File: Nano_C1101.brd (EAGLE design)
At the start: 45.4 x 44.4 mm, 7 parts

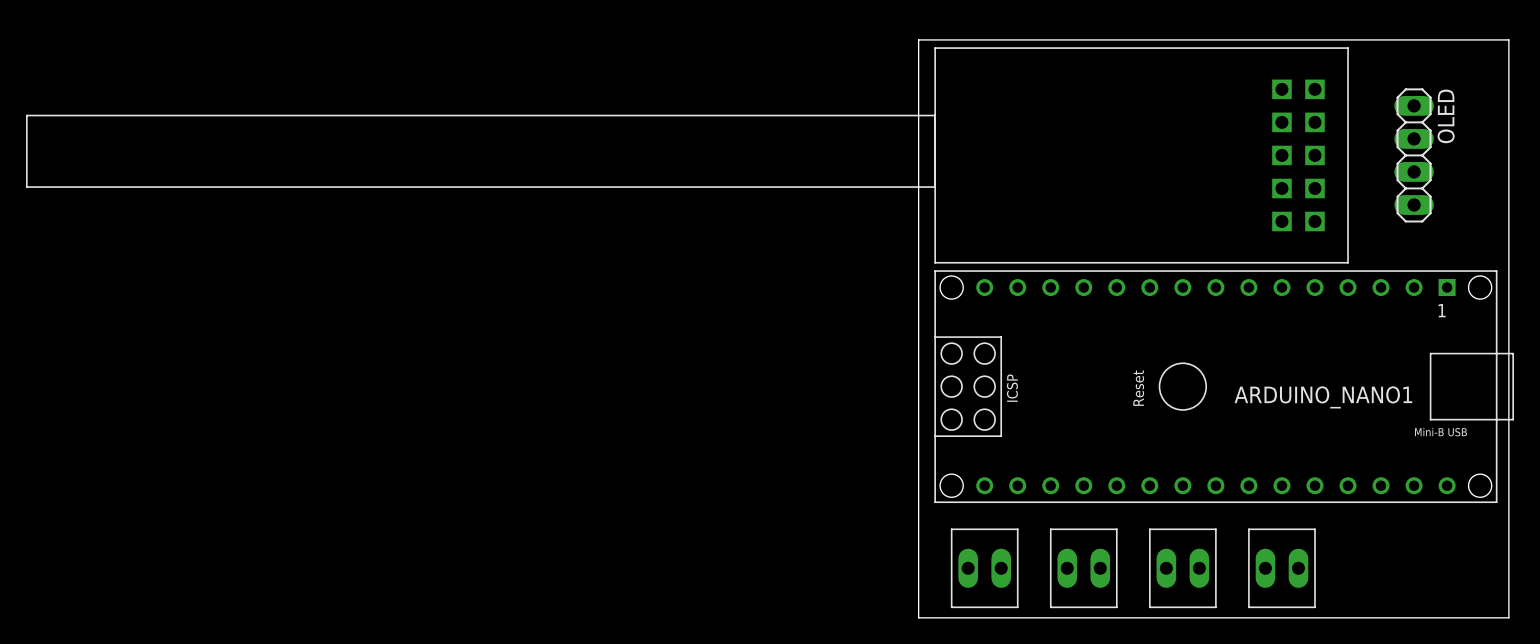
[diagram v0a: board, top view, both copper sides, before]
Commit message: few typos, 3V3 -> 5V
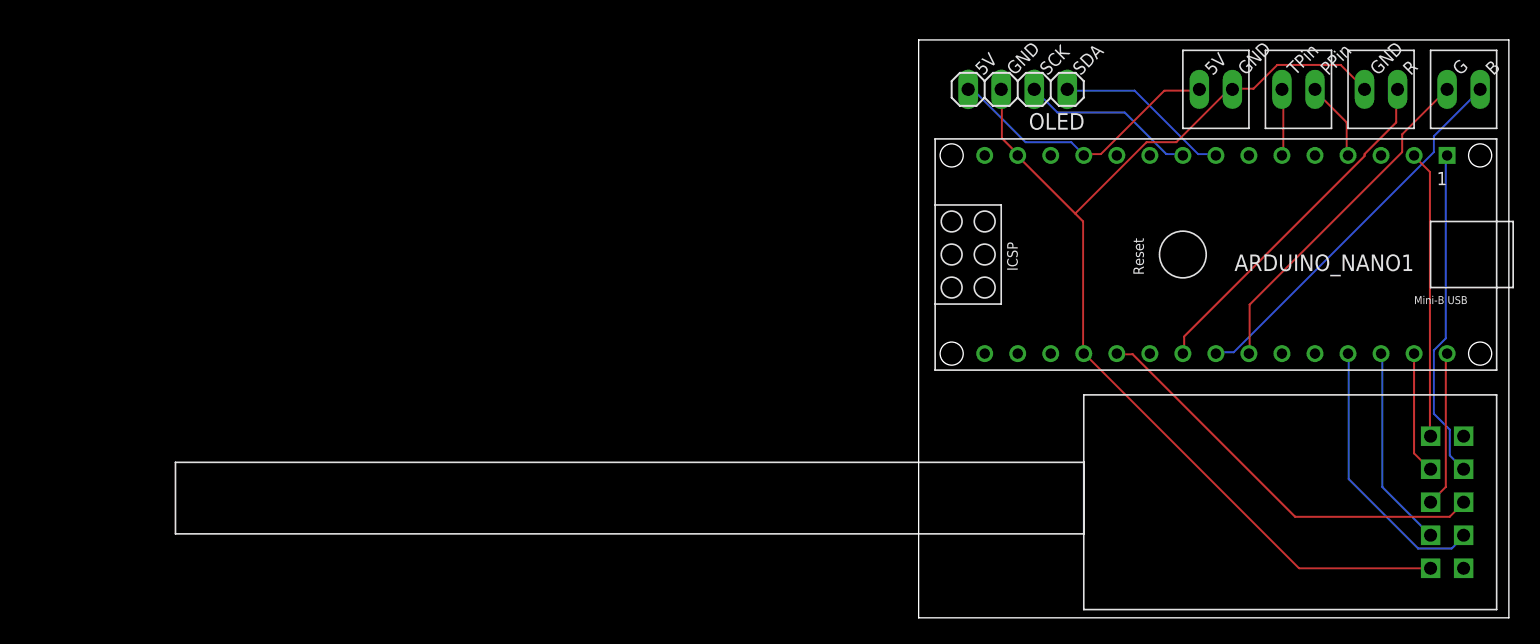
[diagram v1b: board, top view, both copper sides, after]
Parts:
- removed 3.3V--GND: CONRAD567588-2, johannes:CONRAD567588
- added 5V--GND: CONRAD567588-2, johannes:CONRAD567588
- moved TPIN--PPIN 40.4 mm to (29.2, 40.6)
- moved R--GND 39.9 mm to (35.6, 40.6), turned to 180 degrees
- moved G--B 39.4 mm to (41.9, 40.6)
- moved OLED 30.9 mm to (7.62, 40.6), turned to 180 degrees
- moved U$1 29.0 mm to (41.9, 3.81)
- moved ARDUINO_NANO1 10.2 mm to (20.3, 27.9)
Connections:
- net 3V3: no longer 3.3V--GND.P$1
- net 5V: now also 5V--GND.P$1
- net GND: now also 5V--GND.P$2; no longer 3.3V--GND.P$2
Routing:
- net GND: track 0.00 -> 84.2 mm
- net GDO2: track 0.00 -> 32.4 mm
- net B-RGB: track 0.00 -> 29.5 mm
- net R-RGB: track 0.00 -> 27.2 mm
- net G-RGB: track 0.00 -> 26.6 mm
- net SCLK: track 0.00 -> 25.5 mm
- net 3V3: track 0.00 -> 22.1 mm
- net 5V: track 0.00 -> 22.1 mm
- net GDO0: track 0.00 -> 21.2 mm
- net CSN: track 0.00 -> 15.6 mm
- net SDA: track 0.00 -> 13.7 mm
- net SCK: track 0.00 -> 13.6 mm
- net MISO: track 0.00 -> 12.0 mm
- net MOSI: track 0.00 -> 9.45 mm
- net PPIN: track 0.00 -> 6.13 mm
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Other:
- board text added: "5V"
- board text added: "B"
- board text added: "G"
- board text added: "GND"
- board text added: "PPin"
- board text added: "R"
- board text added: "SCK"
- board text added: "SDA"
- board text added: "TPin"

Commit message: Semi-final version of Nano_C1101
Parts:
- added JP1: (no value), adafruit:1X01
- moved 5V--GND 3.81 mm to (26.7, 40.6)
- moved TPIN--PPIN 2.54 mm to (31.8, 40.6)
- moved R--GND 1.27 mm to (36.8, 40.6)
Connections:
- new net N$1: ARDUINO_NANO1.24, JP1.1
- net G-RGB: now also ARDUINO_NANO1.25; no longer ARDUINO_NANO1.24
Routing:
- net N$1: track 0.00 -> 22.4 mm
- net 5V: track 22.1 -> 28.4 mm
- net GND: track 84.2 -> 90.3 mm
- net B-RGB: track 29.5 -> 31.6 mm
- net R-RGB: track 27.2 -> 28.9 mm
- net SCK: track 13.6 -> 14.8 mm
- net TPIN: track 5.16 -> 6.28 mm
- net G-RGB: track 26.6 -> 25.6 mm
- net PPIN: track 6.13 -> 5.16 mm

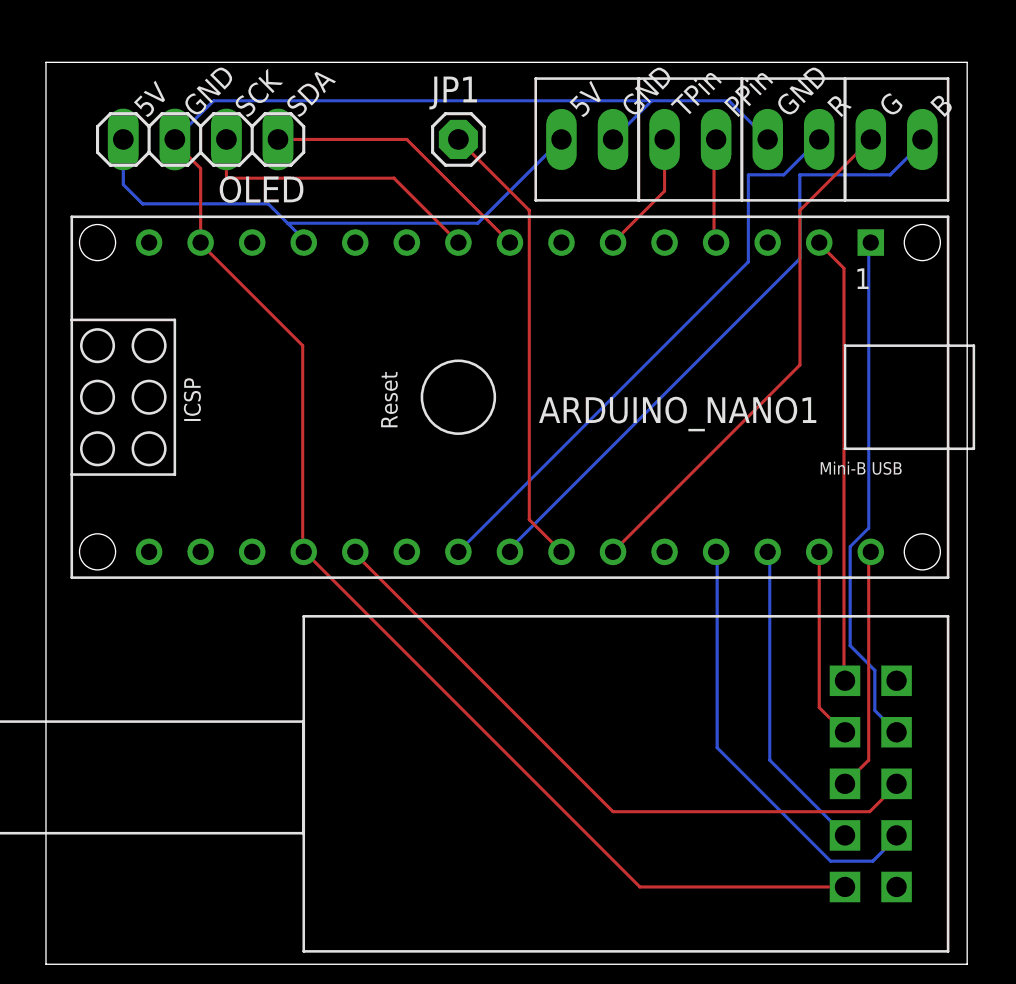
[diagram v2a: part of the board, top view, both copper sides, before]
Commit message: Added resistor and more pins for sensors
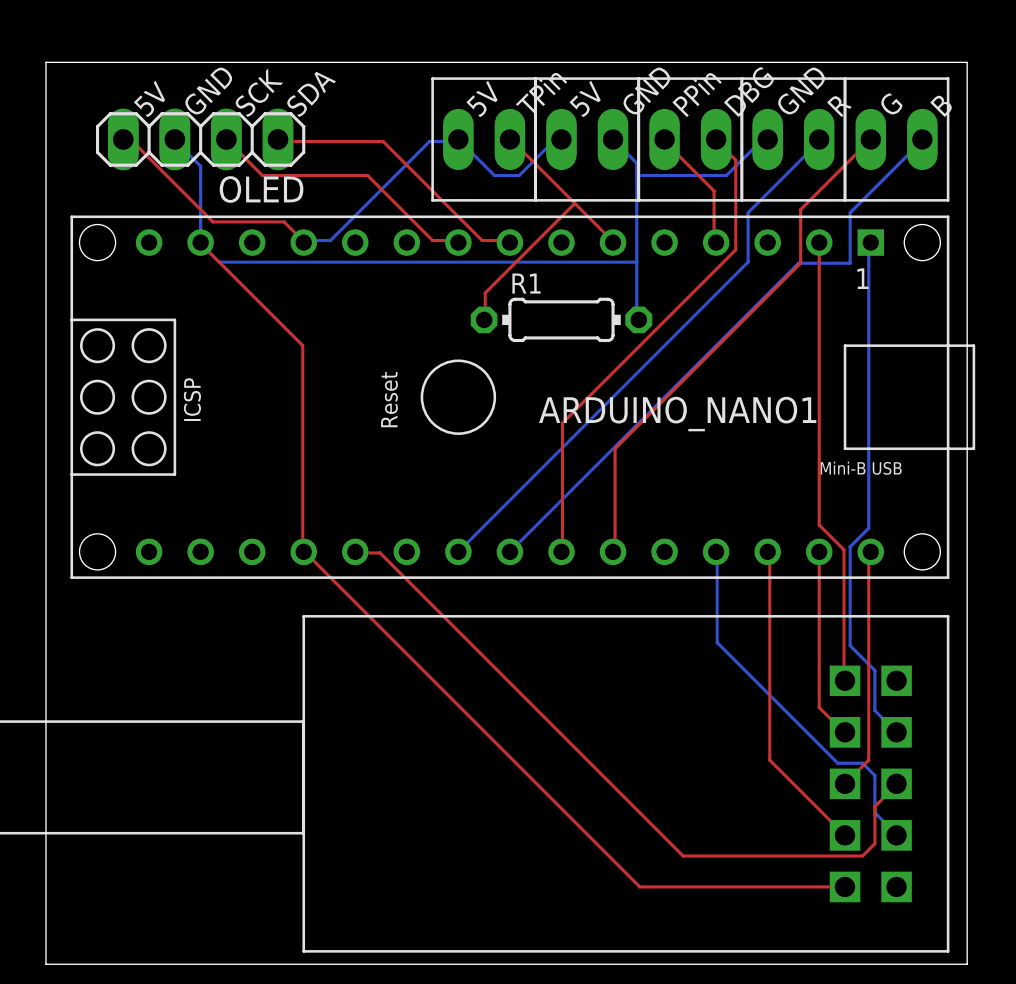
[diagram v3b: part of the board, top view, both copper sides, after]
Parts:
- removed JP1: (no value), adafruit:1X01
- added 5V-TPIN: CONRAD567588-2, johannes:CONRAD567588
- added R1: 1k, rcl:0204/7
- turned DEBUG--PPIN to 180 degrees
- renumbered TPIN--PPIN to DEBUG--PPIN
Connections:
- removed net N$1: ARDUINO_NANO1.24, JP1.1
- new net DEBUG: ARDUINO_NANO1.24, DEBUG--PPIN.P$1
- net 5V: now also 5V-TPIN.P$1
- net GND: now also R1.2
- net TPIN: now also 5V-TPIN.P$2, R1.1; no longer DEBUG--PPIN.P$1
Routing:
- net DEBUG: track 0.00 -> 24.3 mm
- net N$1: track 22.4 -> 0.00 mm
- net TPIN: track 6.28 -> 14.9 mm
- net GND: track 90.3 -> 95.0 mm
- net GDO0: track 21.4 -> 18.4 mm
- net GDO2: track 32.6 -> 35.5 mm
- net B-RGB: track 31.6 -> 30.2 mm
- net SCK: track 14.8 -> 13.6 mm
- net R-RGB: track 28.9 -> 27.7 mm
- net 5V: track 28.4 -> 27.4 mm
- net PPIN: track 5.16 -> 6.13 mm
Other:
- board text added: "DBG"

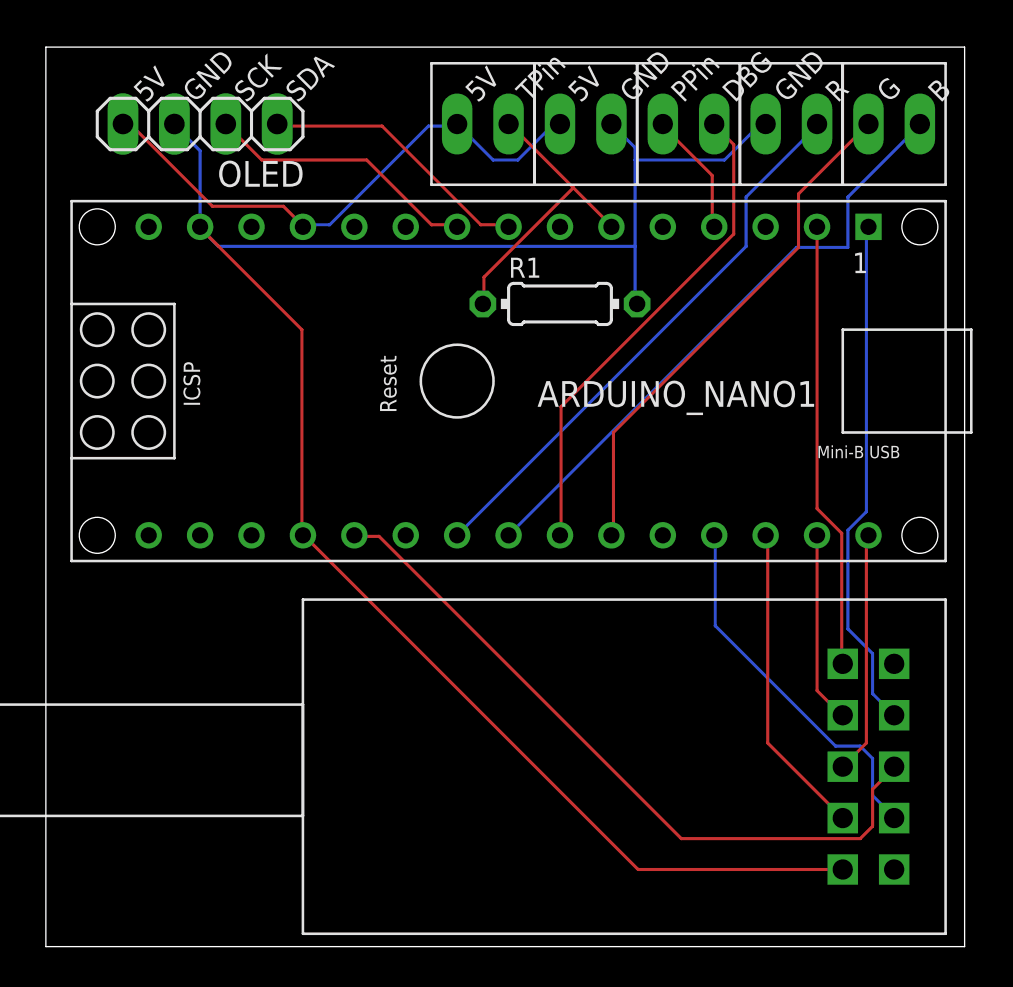
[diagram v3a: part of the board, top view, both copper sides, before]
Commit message: Some more clearance in Nano_C1101.brd
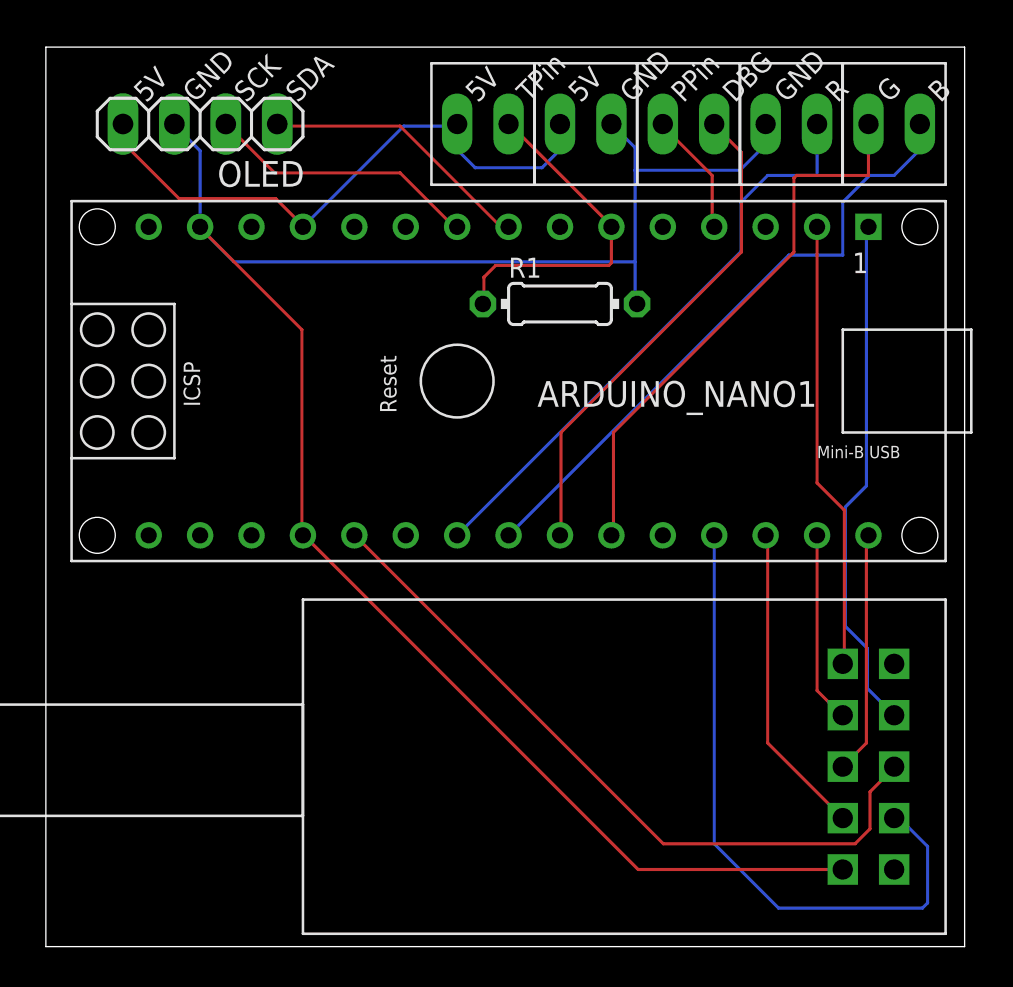
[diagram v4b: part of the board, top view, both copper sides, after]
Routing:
- net GDO0: track 18.4 -> 32.2 mm
- net 5V: track 27.4 -> 29.7 mm
- net TPIN: track 14.9 -> 17.0 mm
- net G-RGB: track 25.6 -> 27.7 mm
- net R-RGB: track 27.7 -> 29.1 mm
- net GND: track 95.0 -> 96.1 mm
- net B-RGB: track 30.2 -> 31.0 mm

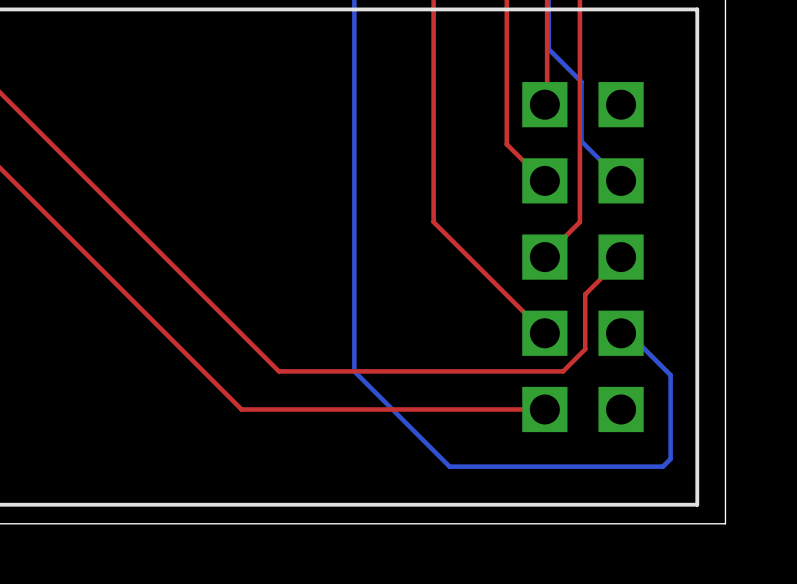
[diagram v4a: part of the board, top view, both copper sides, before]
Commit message: Added text on PCB
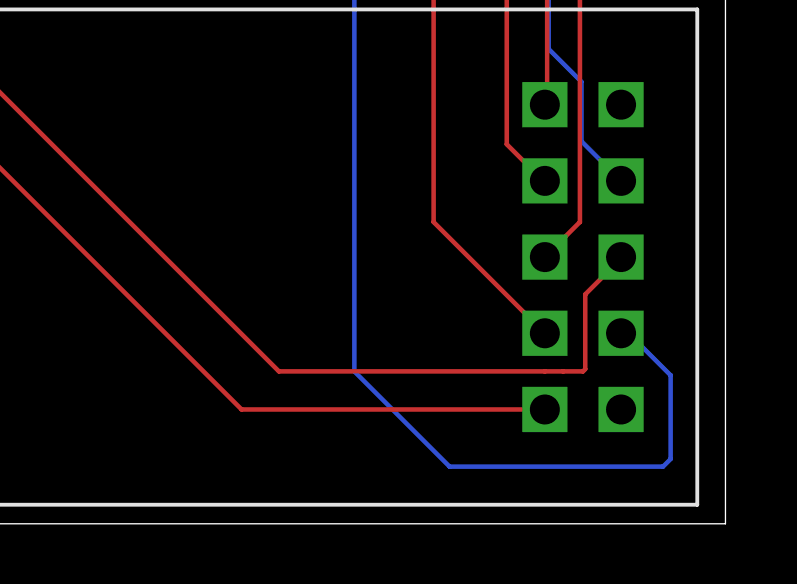
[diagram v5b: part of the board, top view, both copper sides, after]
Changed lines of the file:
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@@
 <wire x1="15.3162" y1="20.2692" x2="15.24" y2="20.2692" width="0.1524" layer="1"/>
 <wire x1="30.5054" y1="5.08" x2="15.3162" y2="20.2692" width="0.1524" layer="1"/>
-<wire x1="39.9796" y1="5.08" x2="30.5054" y2="5.08" width="0.1524" layer="1"/>
-<wire x1="40.7162" y1="5.8166" x2="39.9796" y2="5.08" width="0.1524" layer="1"/>
-<wire x1="40.7162" y1="7.6454" x2="40.7162" y2="5.8166" width="0.1524" layer="1"/>
-<wire x1="41.91" y1="8.8392" x2="40.7162" y2="7.6454" width="0.1524" layer="1"/>
+<wire x1="39.9796" y1="5.08" x2="39.37" y2="5.08" width="0.1524" layer="1"/>
+<wire x1="39.37" y1="5.08" x2="30.5054" y2="5.08" width="0.1524" layer="1"/>
+<wire x1="40.7162" y1="7.6454" x2="41.91" y2="8.8392" width="0.1524" layer="1"/>
 <wire x1="15.24" y1="20.2692" x2="15.24" y2="20.32" width="0.1524" layer="1"/>
 <wire x1="41.91" y1="8.8392" x2="41.91" y2="8.89" width="0.1524" layer="1"/>
+<wire x1="39.9796" y1="5.08" x2="40.64" y2="5.08" width="0.1524" layer="1"/>
+<wire x1="40.64" y1="5.08" x2="40.7162" y2="5.1562" width="0.1524" layer="1"/>
+<wire x1="40.7162" y1="5.1562" x2="40.7162" y2="7.6454" width="0.1524" layer="1"/>
 </signal>
 <signal name="SDA">
